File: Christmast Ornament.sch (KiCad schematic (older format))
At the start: 54 parts, among them J1 USB_OTG, J2 CONN_01X06, Q1 8205A, Q2 SI2302, Q3 BC817, SW1 SW_Push, SW2 SW_Push, U1 TP4056, U10 WS2812b, U2 HT7833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

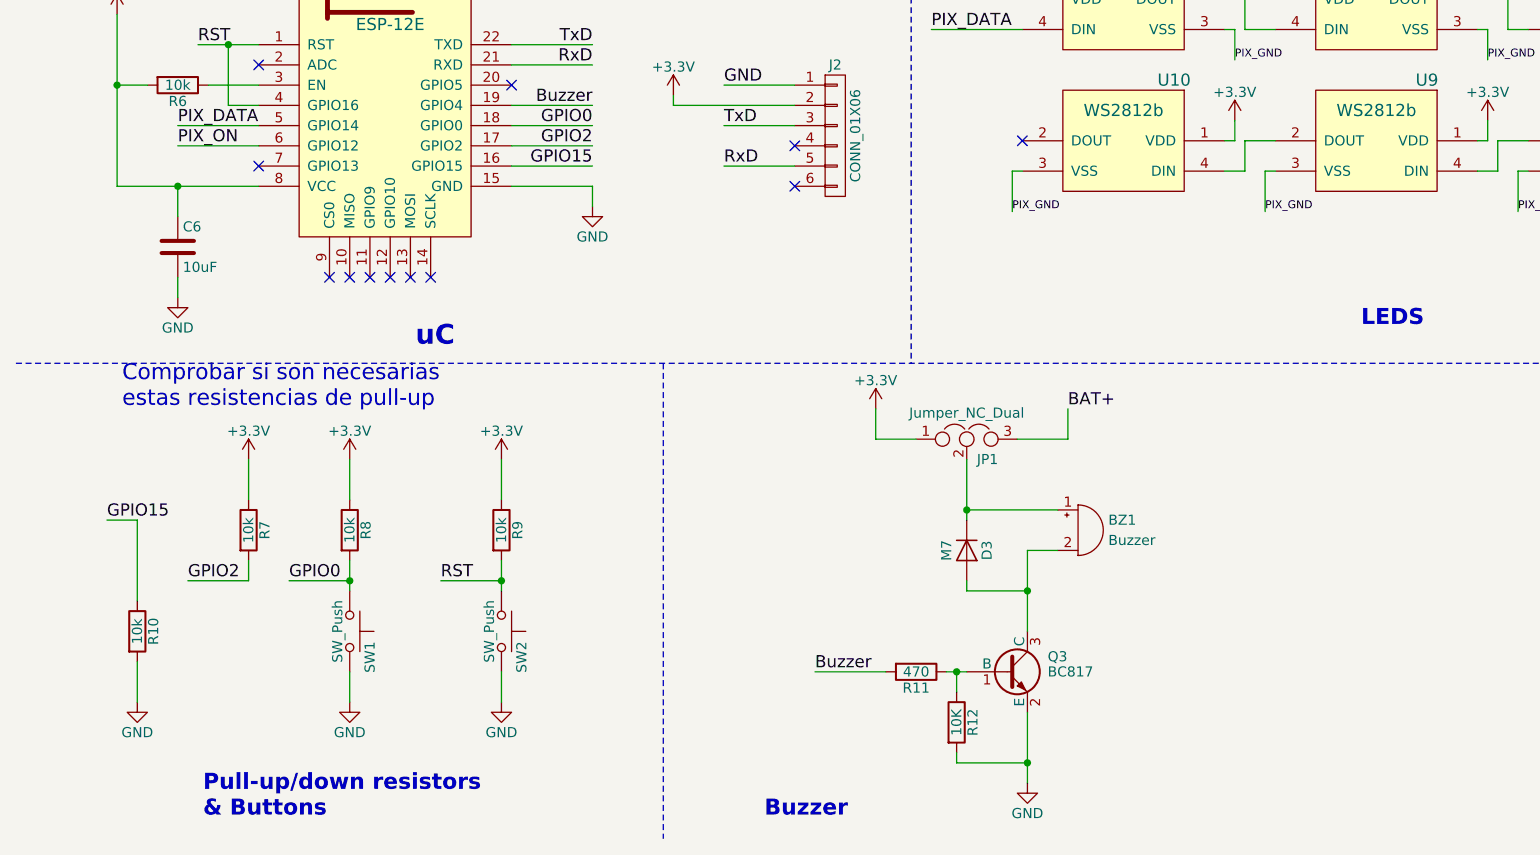
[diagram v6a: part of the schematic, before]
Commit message: Components added to reset button
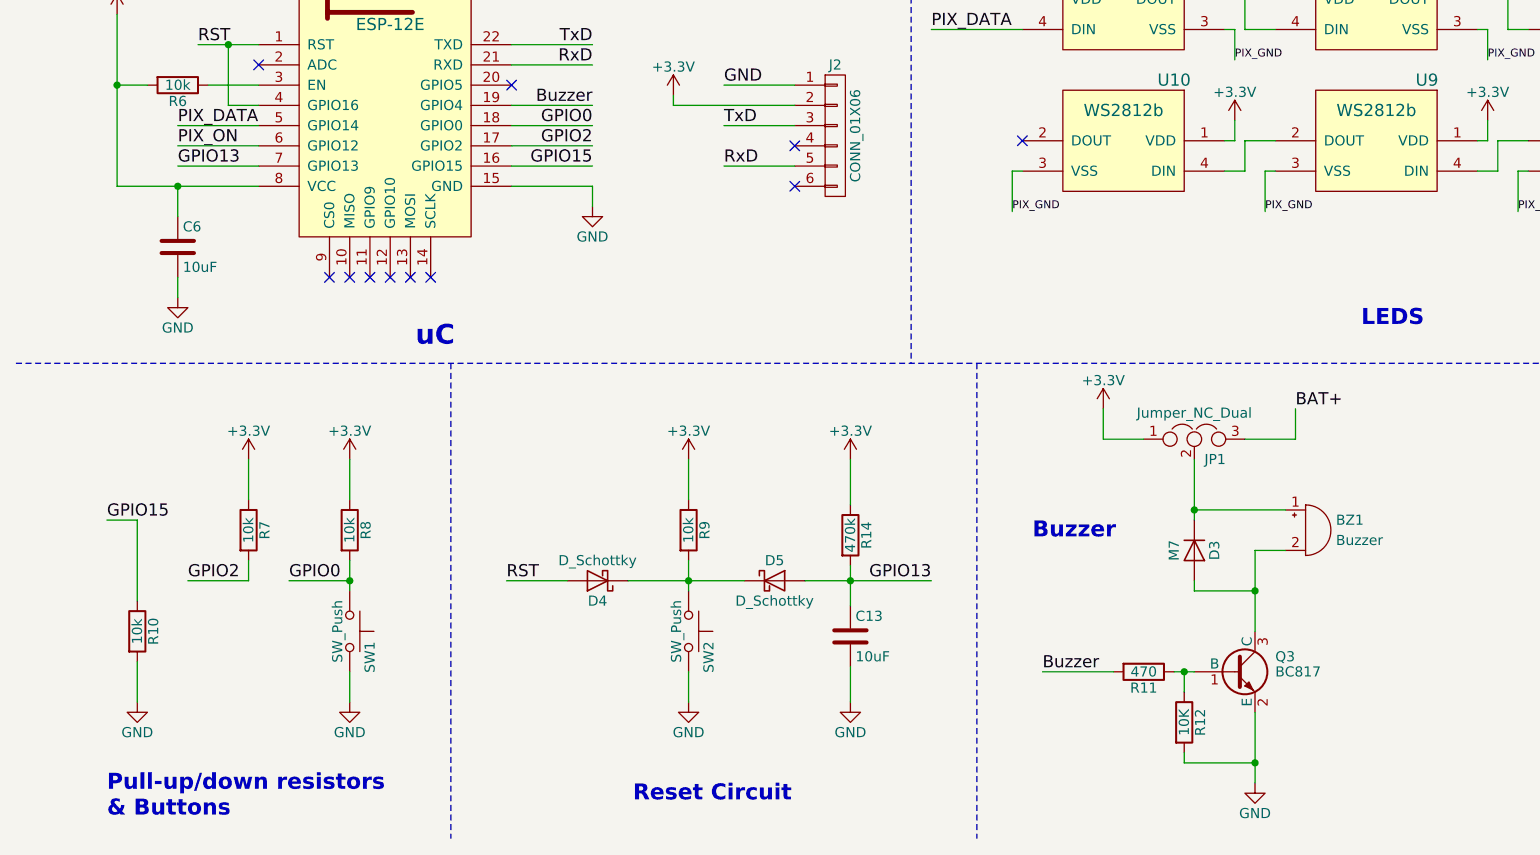
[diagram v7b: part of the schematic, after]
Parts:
- added C13: 10uF, Capacitors_SMD:C_0805_HandSoldering, symbol C
- added D4, D5: D_Schottky, Diodes_SMD:D_0805, symbol D_Schottky
- added R14: 470k, Resistors_SMD:R_0805_HandSoldering, symbol R
- Q2, Q3: footprint TO_SOT_Packages_SMD:SOT-23 -> TO_SOT_Packages_SMD:SOT-23_Handsoldering
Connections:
- net +3V3: now also R14.1
- net GND: now also C13.2
- net RST: now also D4.2 (A); no longer R9.2, SW2.1
- net GPIO13: now reaches U4.7 (GPIO13)
- net GPIO13: now also C13.1, D5.2 (A), R14.2
- new net: D4.1 (K), D5.1 (K), R9.2, SW2.1
- no-connect marks 19 -> 18
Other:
- note added: "Reset Circuit"
- note removed: "Comprobar si son necesarias \nestas resistencias de pull-up"
- moved on the sheet: BZ1, D3, JP1, Q3, R11, R12, R9, SW2

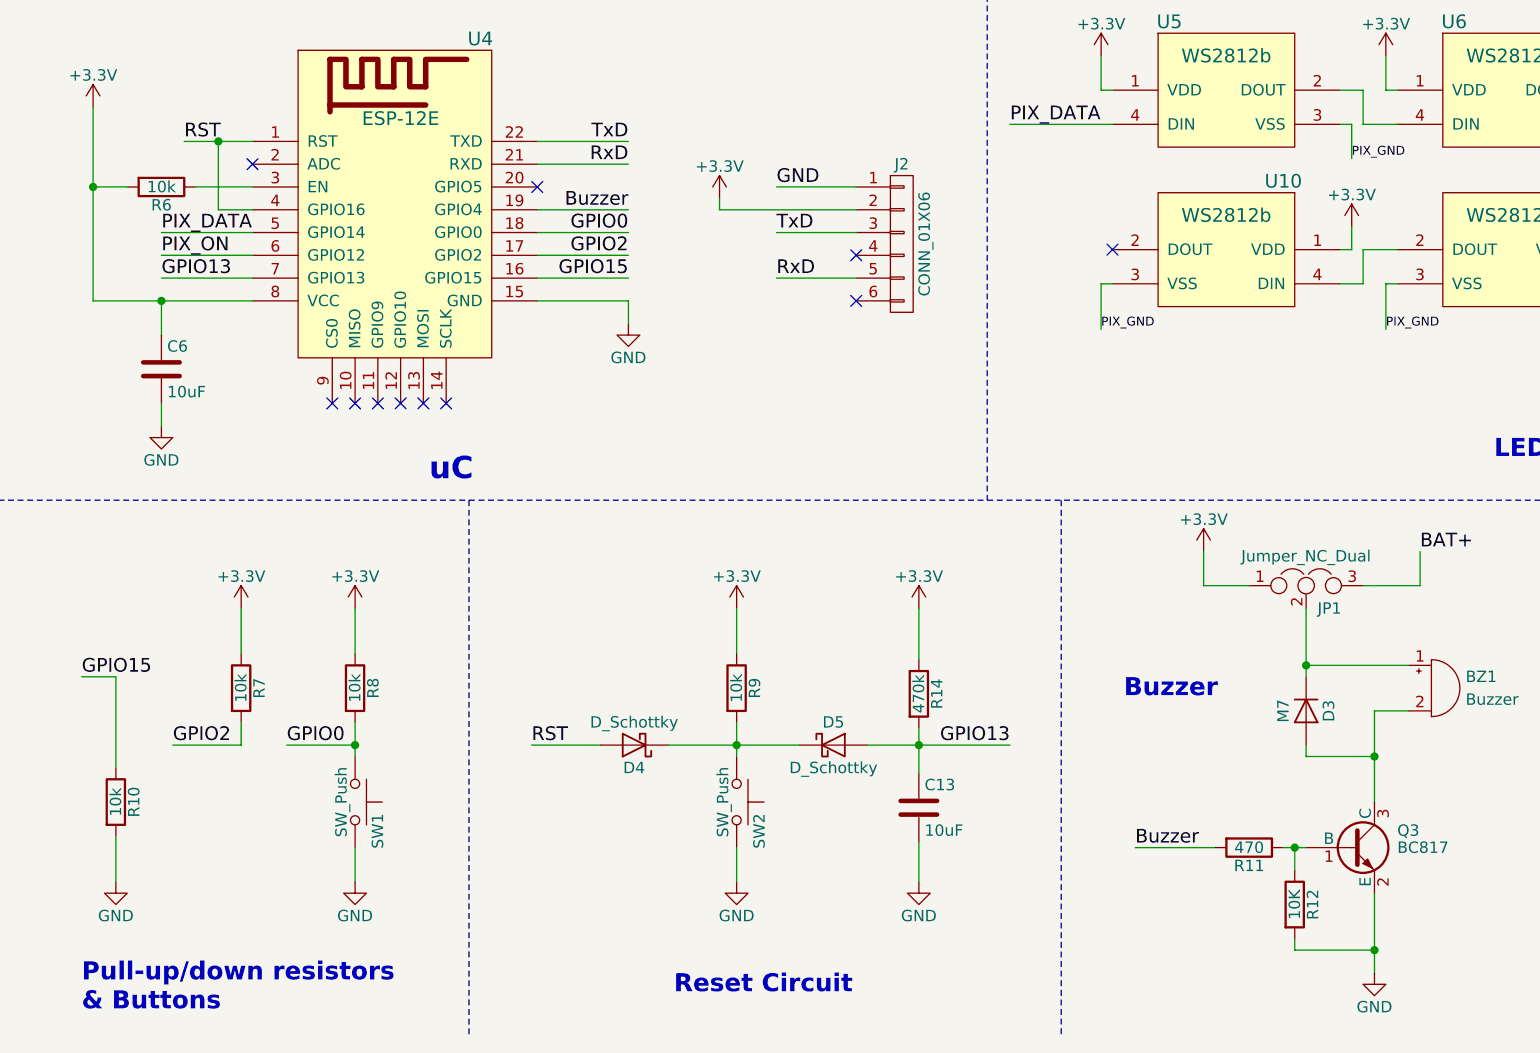
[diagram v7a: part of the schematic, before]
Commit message: capInput routed and R12 deleted
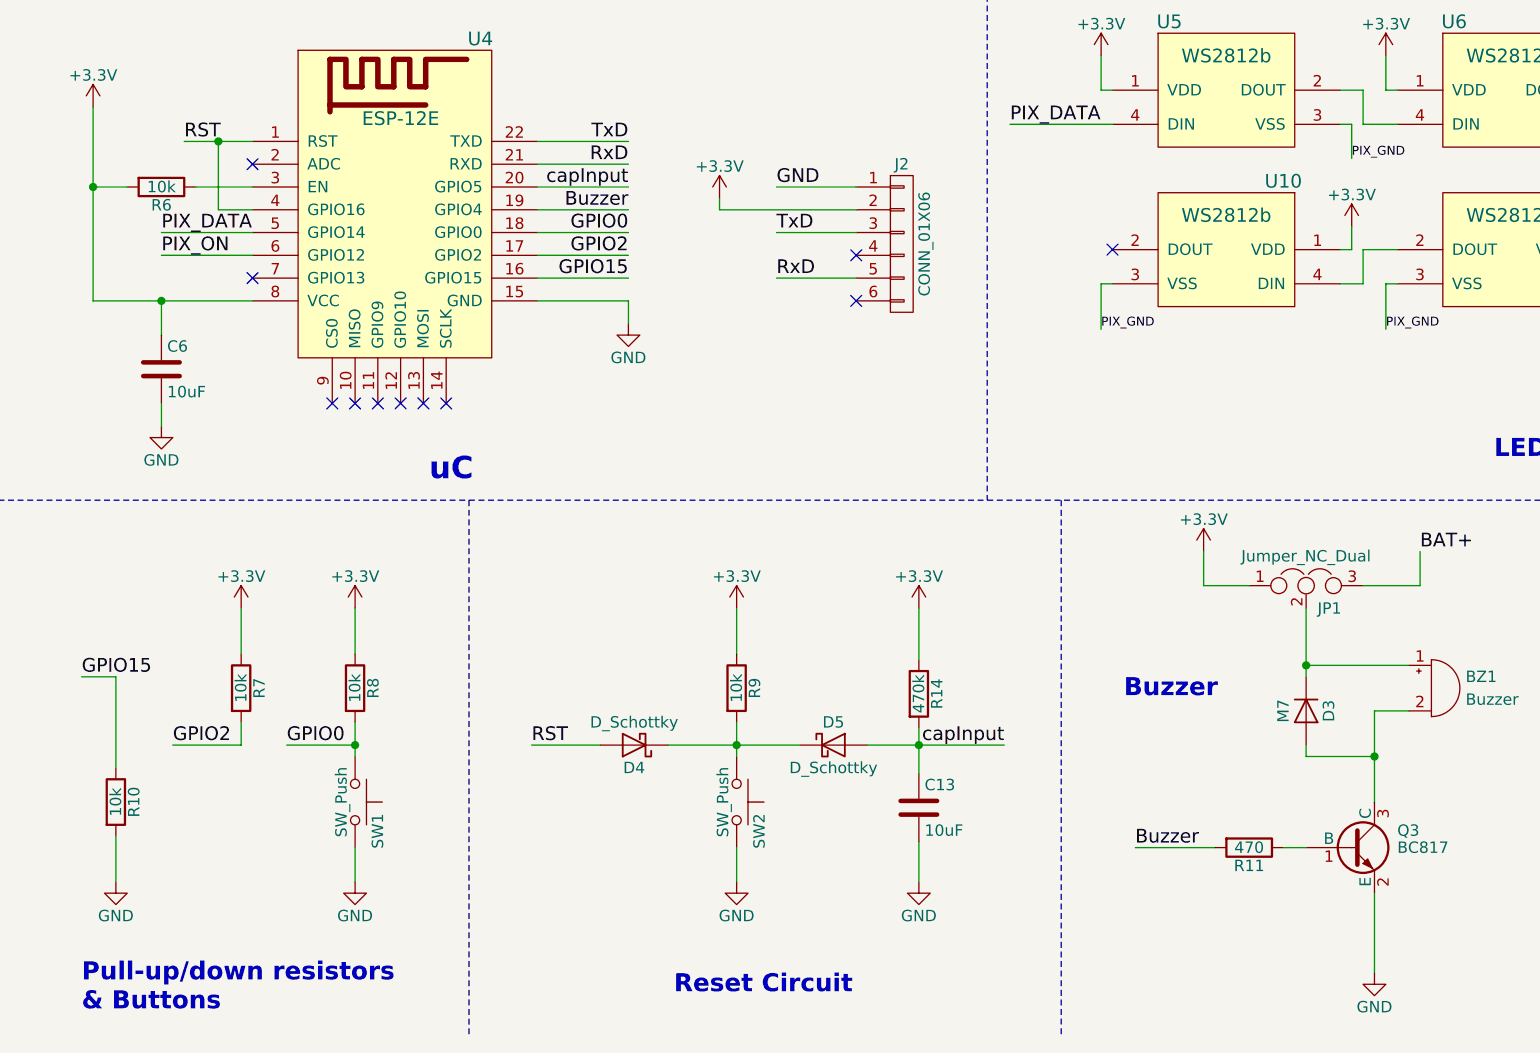
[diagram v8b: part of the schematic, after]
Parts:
- removed R12: 10K, Resistors_SMD:R_0805_HandSoldering, symbol R
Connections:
- net capInput: now reaches U4.20 (GPIO5)
- net capInput: now also C13.1, D5.2 (A), R14.2
- removed net GPIO13: C13.1, D5.2 (A), R14.2, U4.7 (GPIO13)
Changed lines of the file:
@@
 GPIO15
 NoConn ~ 1650 3950
-NoConn ~ 2900 4050
+NoConn ~ 1650 4450
 NoConn ~ 2000 5000
 NoConn ~ 2100 5000
@@
 $EndComp
 $Comp
-L R R12
-U 1 1 5B0A0BB8
-P 6225 7200
-F 0 "R12" V 6305 7200 50  0000 C CNN
-F 1 "10K" V 6225 7200 50  0000 C CNN
-F 2 "Resistors_SMD:R_0805_HandSoldering" V 6155 7200 50  0001 C CNN
-F 3 "" H 6225 7200 50  0001 C CNN
-	1    6225 7200
-	1    0    0    -1
-$EndComp
-$Comp
 L Jumper_NC_Dual JP1
 U 1 1 5B0A20AB
@@
 	6575 7150 6575 7500
 Wire Wire Line
-	6225 7050 6225 6950
-Connection ~ 6225 6950
-Wire Wire Line
-	6225 7350 6225 7400
-Wire Wire Line
-	6225 7400 6575 7400
-Connection ~ 6575 7400
-Wire Wire Line
 	5825 5650 5825 5800
 Wire Wire Line
@@
 Wire Wire Line
 	4575 6425 4575 6625
-Wire Wire Line
-	4350 6500 4975 6500
 $Comp
 L C C13
@@
 Text Notes 3500 7600 0    79   ~ 16
 Reset Circuit
-Wire Wire Line
-	1650 4450 1250 4450
-Text Label 1250 4450 0    60   ~ 0
-GPIO13
-Text Label 4975 6500 2    60   ~ 0
-GPIO13
+Text Label 3300 4050 2    60   ~ 0
+capInput
+Text Label 4950 6500 2    60   ~ 0
+capInput
+Wire Wire Line
+	4350 6500 4950 6500
+Wire Wire Line
+	3300 4050 2900 4050
 $EndSCHEMATC
